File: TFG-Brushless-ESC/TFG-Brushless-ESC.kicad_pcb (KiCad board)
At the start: 4 copper layers, 110.5 x 44 mm, 147 parts, among them J1 V, J2 USB C Receptacle, J3 HALL SENSORS, J4 SWD-I2C, J5 24V IN, J6 U, J7 W, Q1 TK58E06N1, Q2 TK58E06N1, Q3 TK58E06N1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

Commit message: Added fan control and temp measurement. Not added to pcb yet
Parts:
- removed J1: V, TFG-Brushless-ESC:Screw_Terminal
- removed J7: W, TFG-Brushless-ESC:Screw_Terminal
- removed R44: 10k, Resistor_SMD:R_0603_1608Metric
- added C23: 100n, Capacitor_SMD:C_0603_1608Metric, F.Cu at (145.6, 35.2)
- added C32: 10u, Capacitor_SMD:CP_Elec_4x5.4, F.Cu at (151.5, 36.9)
- added J8: ~, TFG-Brushless-ESC:Screw_Terminal, F.Cu at (158.4, 72.9)
- added J9: ~, TFG-Brushless-ESC:Screw_Terminal, F.Cu at (188.2, 72.9)
- added L2: 30mm fan, Connector_PinHeader_1.00mm:PinHeader_1x02_P1.00mm_Vertical, F.Cu at (162.0, 36.6)
- added Q7: DMG3402L, Package_TO_SOT_SMD:SOT-23, F.Cu at (158.1, 37.4)
- added R47: 10k 1%, Resistor_SMD:R_0603_1608Metric, F.Cu at (145.6, 37.7)
- added R48: 10k, Resistor_SMD:R_0603_1608Metric, F.Cu at (145.6, 40.2)
- added R49: 22R, Resistor_SMD:R_0603_1608Metric, F.Cu at (145.6, 42.7)
- added R50: 10k, Resistor_SMD:R_0603_1608Metric, F.Cu at (160.9, 63.9)
- added R51: 10k, Resistor_SMD:R_0603_1608Metric, F.Cu at (190.6, 63.9)
- added TH1: 100k, Connector_PinHeader_1.00mm:PinHeader_1x02_P1.00mm_Vertical, F.Cu at (154.1, 41.3)
- added U11: ADC081C021, Package_TO_SOT_SMD:SOT-23-6, F.Cu at (150.0, 42.1)
- J6: value U -> ~
- R43: value 10k -> 100R; footprint Resistor_SMD:R_0603_1608Metric -> Resistor_SMD:R_0805_2012Metric
- moved R43 22.9 mm to (158.1, 41.1), turned to 0 degrees
- moved J6 0.20 mm to (128.7, 72.9), turned to 0 degrees
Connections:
- net /U renamed /Half-Bridge-U/PHASE_OUT
- net /W renamed /Half-Bridge-W/PHASE_OUT
- C30 pad 2: /V -> /Half-Bridge-V/PHASE_OUT
- C31 pad 2: /V -> /Half-Bridge-V/PHASE_OUT
- D18 pad 2: /V -> /Half-Bridge-V/PHASE_OUT
- D19 pad 2: /V -> /Half-Bridge-V/PHASE_OUT
- Q3 pad 3: /V -> /Half-Bridge-V/PHASE_OUT
- Q4 pad 2: /V -> /Half-Bridge-V/PHASE_OUT
- R28 pad 2: /V -> /Half-Bridge-V/PHASE_OUT
- R29 pad 2: /V -> /Half-Bridge-V/PHASE_OUT
- R43 pad 1: GND -> /PB7
- R43 pad 2: /V -> Net-(Q7-G)
- U6 pad 6: /V -> /Half-Bridge-V/PHASE_OUT
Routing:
- net /V: track 41.8 -> 0.00 mm, vias 5 -> 0
- net /Half-Bridge-V/PHASE_OUT: track 0.00 -> 41.8 mm, vias 0 -> 5
- net GND: track 195.6 -> 195.5 mm, vias 172 -> 186
- added copper zone on B.Cu, net /Half-Bridge-V/PHASE_OUT
- added copper zone on F.Cu, net /Half-Bridge-V/PHASE_OUT
- added copper zone on In1.Cu, net /Half-Bridge-V/PHASE_OUT
- added copper zone on In2.Cu, net /Half-Bridge-V/PHASE_OUT
- removed copper zone on B.Cu, net /V
- removed copper zone on F.Cu, net /V
- removed copper zone on In1.Cu, net /V
- removed copper zone on In2.Cu, net /V

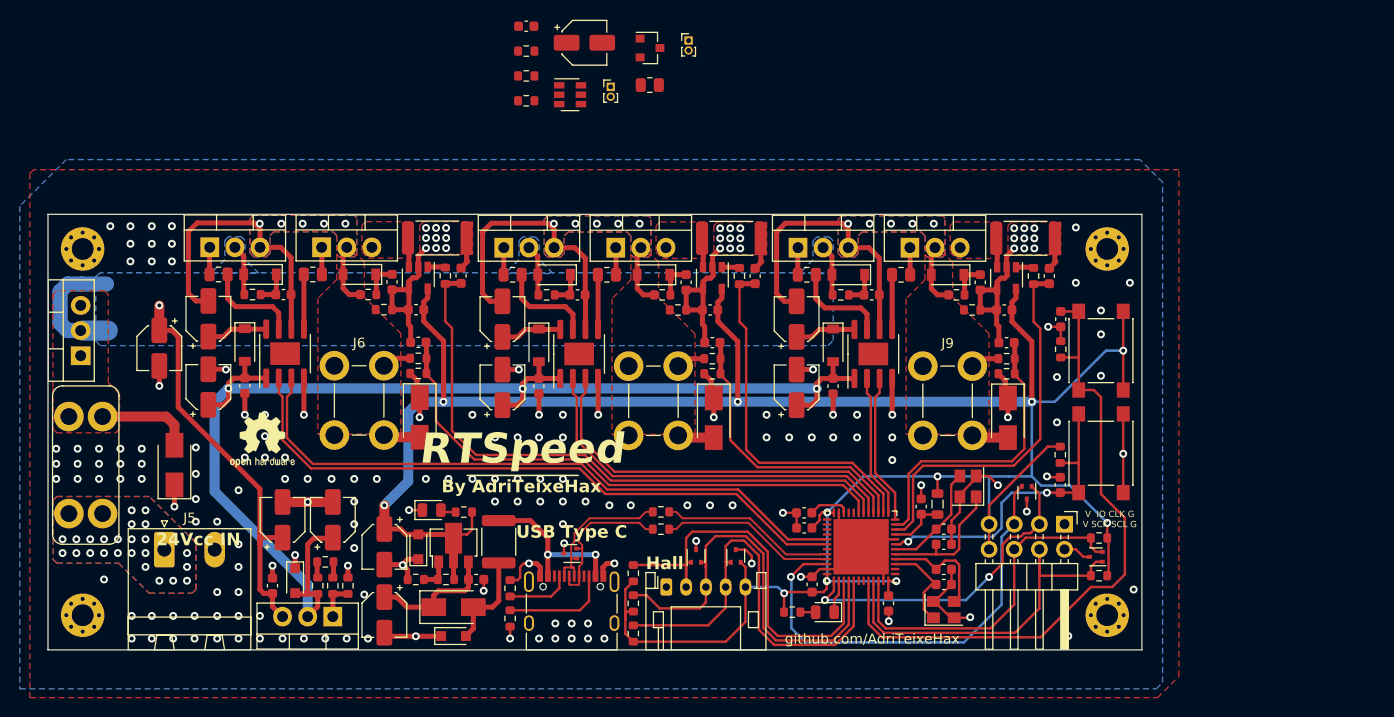
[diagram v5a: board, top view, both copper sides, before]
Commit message: Added temperature sensors per phase and adc
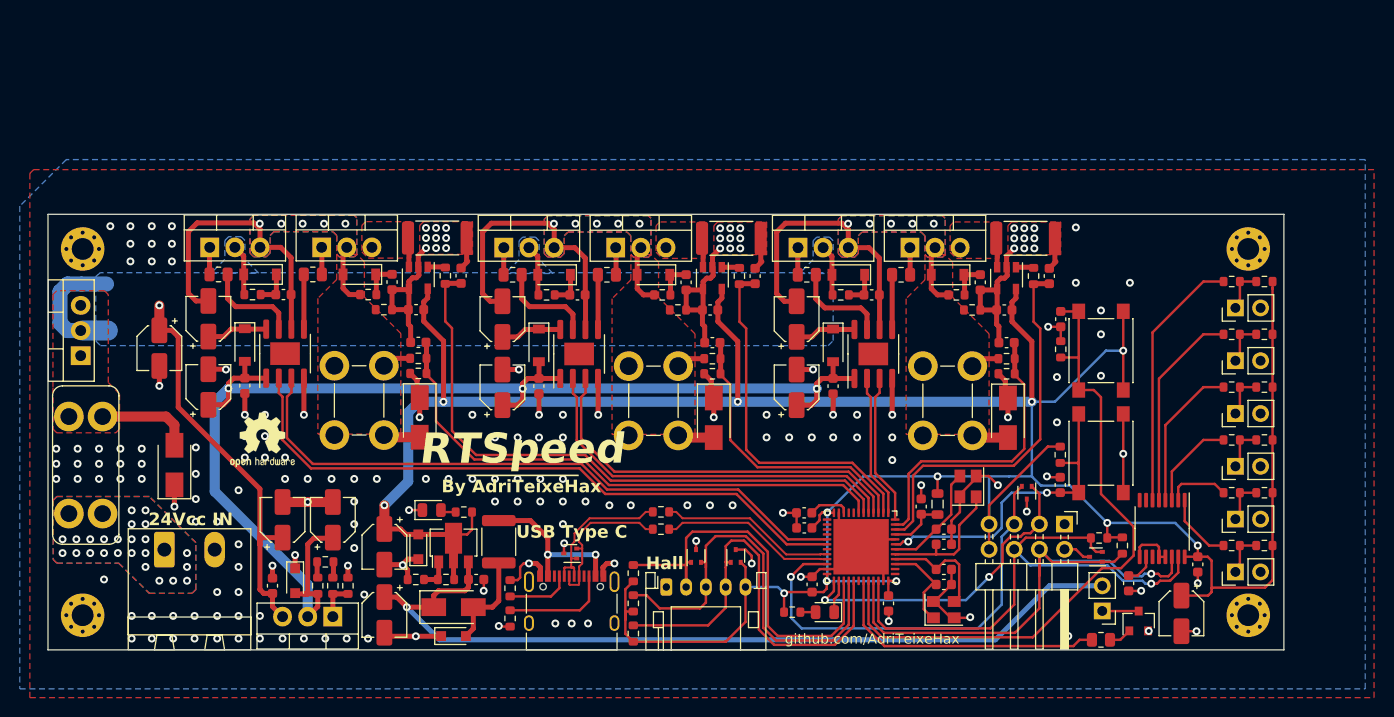
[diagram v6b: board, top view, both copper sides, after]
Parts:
- removed C23: 100n, Capacitor_SMD:C_0603_1608Metric
- removed C32: 10u, Capacitor_SMD:CP_Elec_4x5.4
- removed R47: 10k 1%, Resistor_SMD:R_0603_1608Metric
- removed R48: 10k, Resistor_SMD:R_0603_1608Metric
- removed R49: 22R, Resistor_SMD:R_0603_1608Metric
- removed TH1: 100k, Connector_PinHeader_1.00mm:PinHeader_1x02_P1.00mm_Vertical
- removed U11: ADC081C021, Package_TO_SOT_SMD:SOT-23-6
- added C46: 100n, Capacitor_SMD:C_0603_1608Metric, F.Cu at (206.5, 91.5)
- added C47: 100n, Capacitor_SMD:C_0603_1608Metric, F.Cu at (213.4, 89.6)
- added C48: 10u, Capacitor_SMD:CP_Elec_4x5.4, F.Cu at (211.8, 94.5)
- added R44: 10k 1%, Resistor_SMD:R_0603_1608Metric, F.Cu at (220.2, 87.7)
- added R52: 10k 1%, Resistor_SMD:R_0603_1608Metric, F.Cu at (220.2, 82.3)
- added R53: 22R, Resistor_SMD:R_0603_1608Metric, F.Cu at (216.9, 87.7)
- added R54: 22R, Resistor_SMD:R_0603_1608Metric, F.Cu at (216.9, 82.3)
- added R55: 10k 1%, Resistor_SMD:R_0603_1608Metric, F.Cu at (220.2, 77.0)
- added R56: 10k 1%, Resistor_SMD:R_0603_1608Metric, F.Cu at (220.2, 71.7)
- added R57: 22R, Resistor_SMD:R_0603_1608Metric, F.Cu at (216.9, 77.0)
- added R58: 22R, Resistor_SMD:R_0603_1608Metric, F.Cu at (216.9, 71.7)
- added R59: 10k 1%, Resistor_SMD:R_0603_1608Metric, F.Cu at (220.2, 66.3)
- added R60: 10k 1%, Resistor_SMD:R_0603_1608Metric, F.Cu at (220.2, 61.0)
- added R61: 22R, Resistor_SMD:R_0603_1608Metric, F.Cu at (216.9, 66.3)
- added R62: 22R, Resistor_SMD:R_0603_1608Metric, F.Cu at (216.9, 61.0)
- added TH2: 100k, Connector_PinHeader_2.54mm:PinHeader_1x02_P2.54mm_Vertical, F.Cu at (217.2, 90.3)
- added TH3: 100k, Connector_PinHeader_2.54mm:PinHeader_1x02_P2.54mm_Vertical, F.Cu at (217.2, 85.0)
- added TH4: 100k, Connector_PinHeader_2.54mm:PinHeader_1x02_P2.54mm_Vertical, F.Cu at (217.2, 79.7)
- added TH5: 100k, Connector_PinHeader_2.54mm:PinHeader_1x02_P2.54mm_Vertical, F.Cu at (217.2, 74.3)
- added TH6: 100k, Connector_PinHeader_2.54mm:PinHeader_1x02_P2.54mm_Vertical, F.Cu at (217.2, 69.0)
- added TH7: 100k, Connector_PinHeader_2.54mm:PinHeader_1x02_P2.54mm_Vertical, F.Cu at (217.2, 63.7)
- added U10: ADS7830, Package_SO:TSSOP-16_4.4x5mm_P0.65mm, F.Cu at (209.8, 85.9)
- L2: footprint Connector_PinHeader_1.00mm:PinHeader_1x02_P1.00mm_Vertical -> Connector_PinHeader_2.54mm:PinHeader_1x02_P2.54mm_Vertical
- moved Q7 76.1 mm to (207.5, 95.3), turned to 90 degrees
- moved R43 72.2 mm to (203.7, 97.2)
- moved L2 71.2 mm to (203.8, 94.3), turned to 180 degrees
- moved REF** 14.2 mm to (218.5, 57.7)
- moved REF** 14.2 mm to (218.5, 94.7)
- moved R45 3.85 mm to (205.8, 87.7), turned to 90 degrees
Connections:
- net /VDDA renamed VDDA
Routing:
- net +5V: track 13.0 -> 86.9 mm, vias 0 -> 1
- net +3V3: track 273.2 -> 328.0 mm, vias 11 -> 12
- net /PB7: track 0.00 -> 28.7 mm
- net /Temp. sensors/S6: track 0.00 -> 26.3 mm
- net /Temp. sensors/S5: track 0.00 -> 20.6 mm
- net /I2C_SDA: track 35.2 -> 55.2 mm, vias 0 -> 1
- net /I2C_SCL: track 38.5 -> 56.8 mm, vias 0 -> 1
- net /Temp. sensors/S4: track 0.00 -> 15.0 mm
- net /Temp. sensors/S3: track 0.00 -> 9.44 mm
- net GND: track 195.5 -> 204.2 mm, vias 186 -> 184
- net /Temp. sensors/S1: track 0.00 -> 7.06 mm
- net /Temp. sensors/S2: track 0.00 -> 6.40 mm
- net /Temp. sensors/T6: track 0.00 -> 4.50 mm
- net /Temp. sensors/T3: track 0.00 -> 4.50 mm
- net /Temp. sensors/T2: track 0.00 -> 4.50 mm
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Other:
- board size 110.5 x 44 mm -> 124.9 x 44 mm
- board text removed: "V IO CLK G V SCK SCL G"

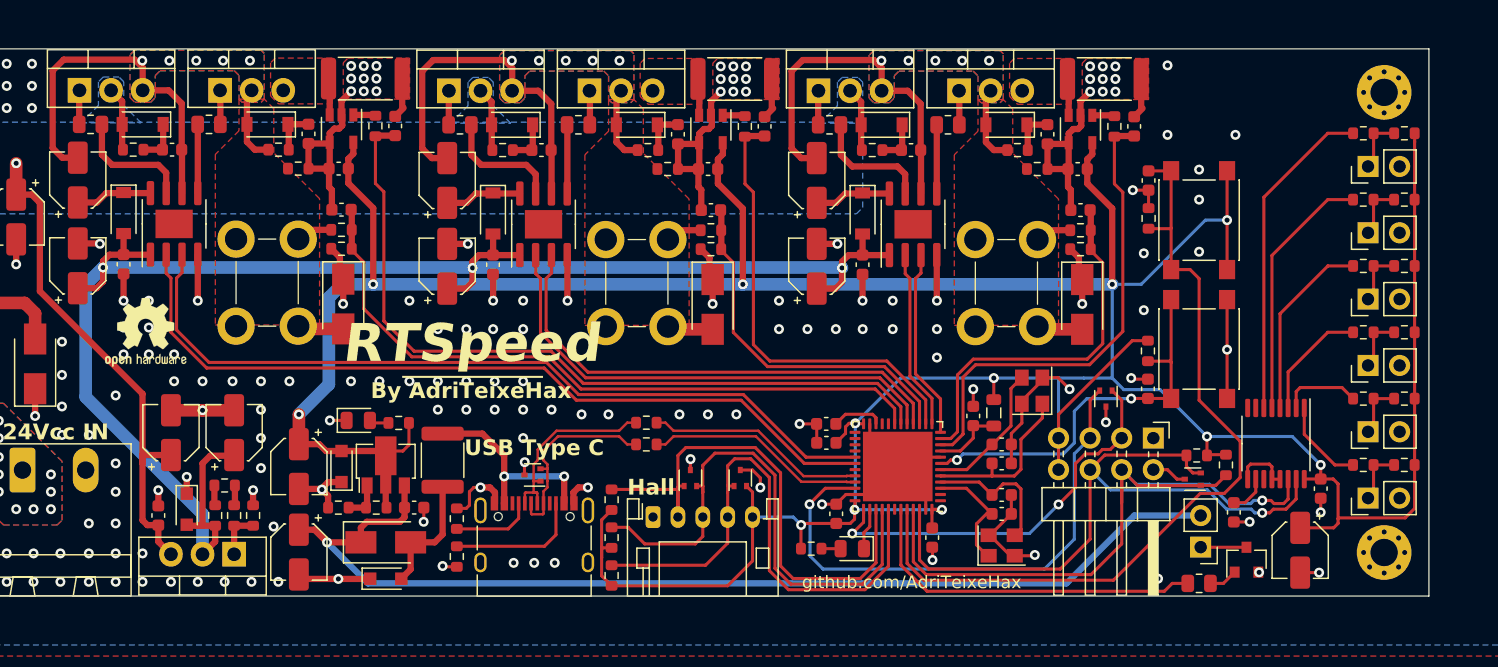
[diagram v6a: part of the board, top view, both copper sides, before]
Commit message: Added pulldown resistors for the half bridge mosfets, fan mosfet and fixed code pinout
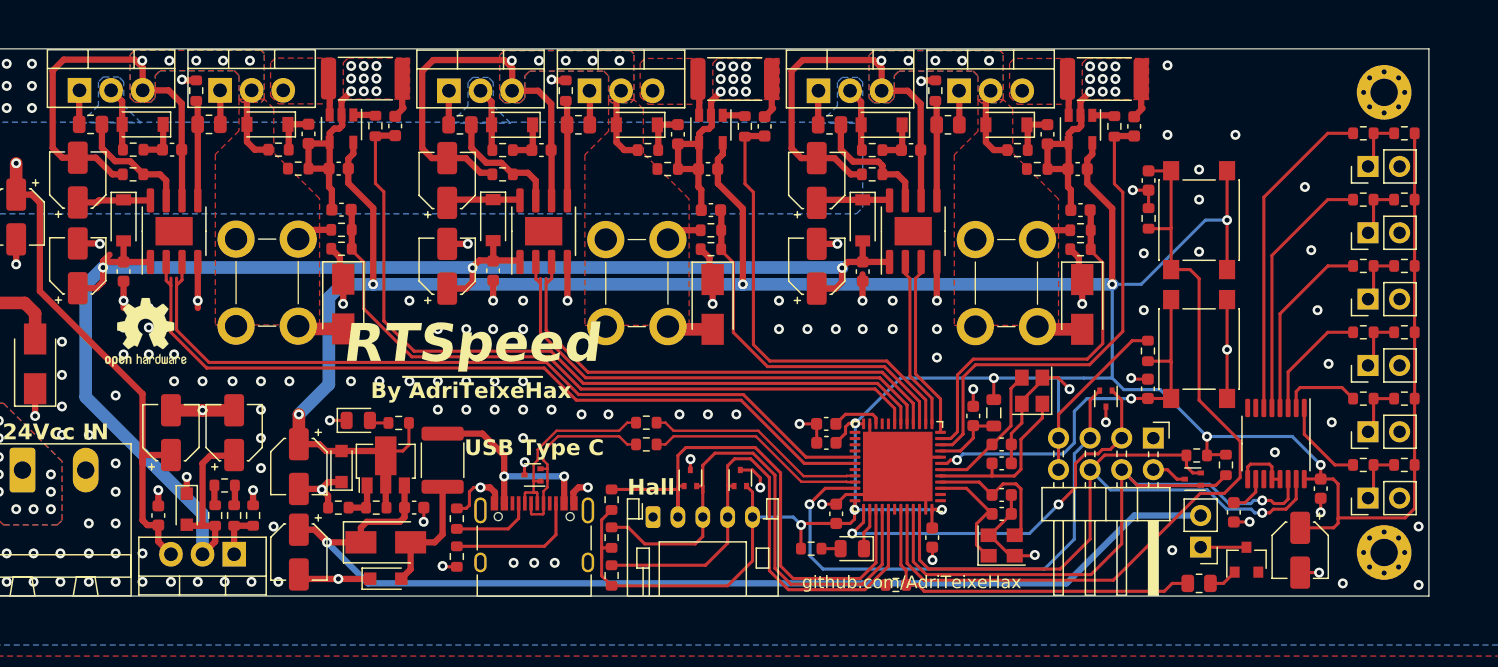
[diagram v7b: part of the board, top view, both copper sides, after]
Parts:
- added R47: 10k, Resistor_SMD:R_0603_1608Metric, F.Cu at (117.9, 64.3)
- added R48: 10k, Resistor_SMD:R_0603_1608Metric, F.Cu at (147.7, 64.3)
- added R49: 10k, Resistor_SMD:R_0603_1608Metric, F.Cu at (177.4, 64.3)
- added R63: 10k, Resistor_SMD:R_0603_1608Metric, F.Cu at (123.0, 57.6)
- added R64: 10k, Resistor_SMD:R_0603_1608Metric, F.Cu at (152.7, 57.6)
- added R65: 10k, Resistor_SMD:R_0603_1608Metric, F.Cu at (182.5, 57.6)
- added R66: 10k, Resistor_SMD:R_0603_1608Metric, F.Cu at (179.3, 97.3)
- moved C20 0.59 mm to (117.2, 72.1)
- moved D13 0.59 mm to (117.2, 68.0)
- moved U4 0.59 mm to (121.2, 68.9)
- moved C38 0.55 mm to (176.6, 72.1)
- moved D21 0.55 mm to (176.6, 68.0)
- moved U6 0.55 mm to (151.0, 68.9)
- moved U8 0.55 mm to (180.7, 68.9)
- moved D17 0.54 mm to (146.9, 68.0)
- moved C29 0.48 mm to (146.9, 72.0)
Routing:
- net /Half-Bridge-U/PHASE_OUT: track 41.8 -> 46.0 mm
- net /Half-Bridge-W/PHASE_OUT: track 41.8 -> 46.0 mm
- net /Half-Bridge-V/PHASE_OUT: track 41.8 -> 46.0 mm
- net GND: track 204.2 -> 207.2 mm, vias 184 -> 196
- net /I2C_SCL: track 56.8 -> 54.1 mm
- net Net-(U8-LO): track 5.53 -> 7.50 mm
- net Net-(U6-LO): track 5.53 -> 7.50 mm
- net Net-(U4-LO): track 5.53 -> 7.47 mm
- net +12V: track 129.1 -> 128.1 mm
- net /PB7: track 28.7 -> 29.4 mm

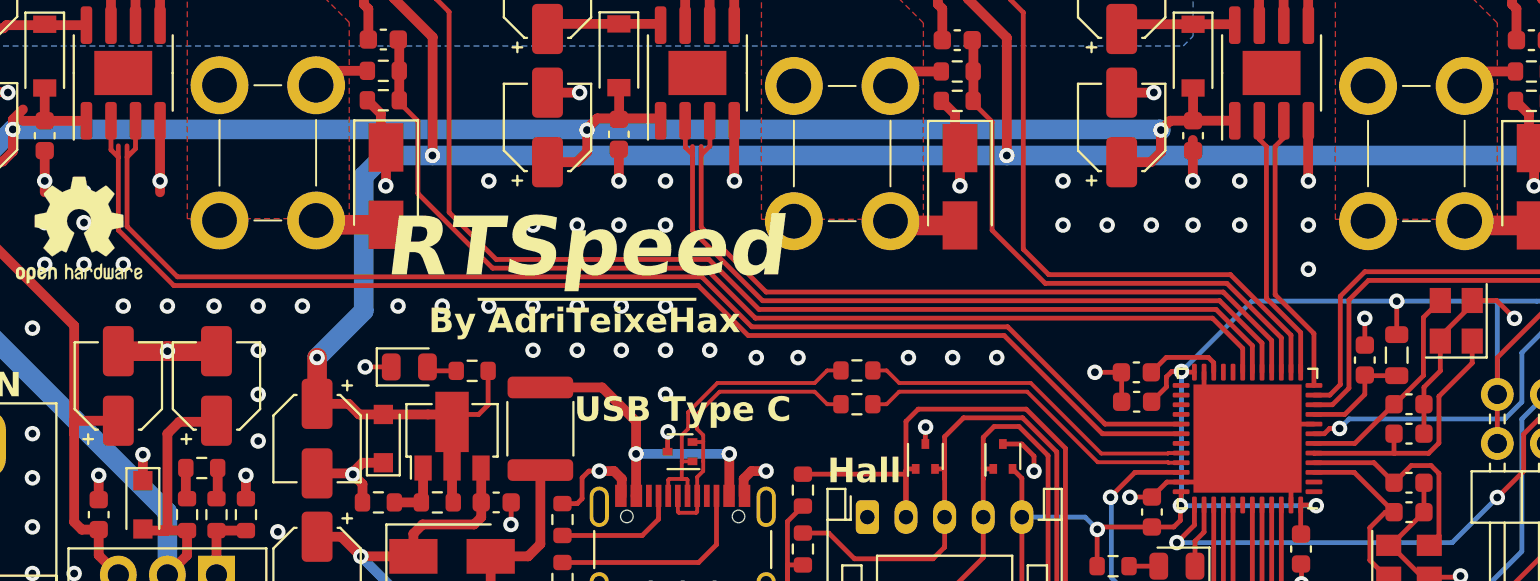
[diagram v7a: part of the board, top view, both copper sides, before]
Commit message: more separation between traces
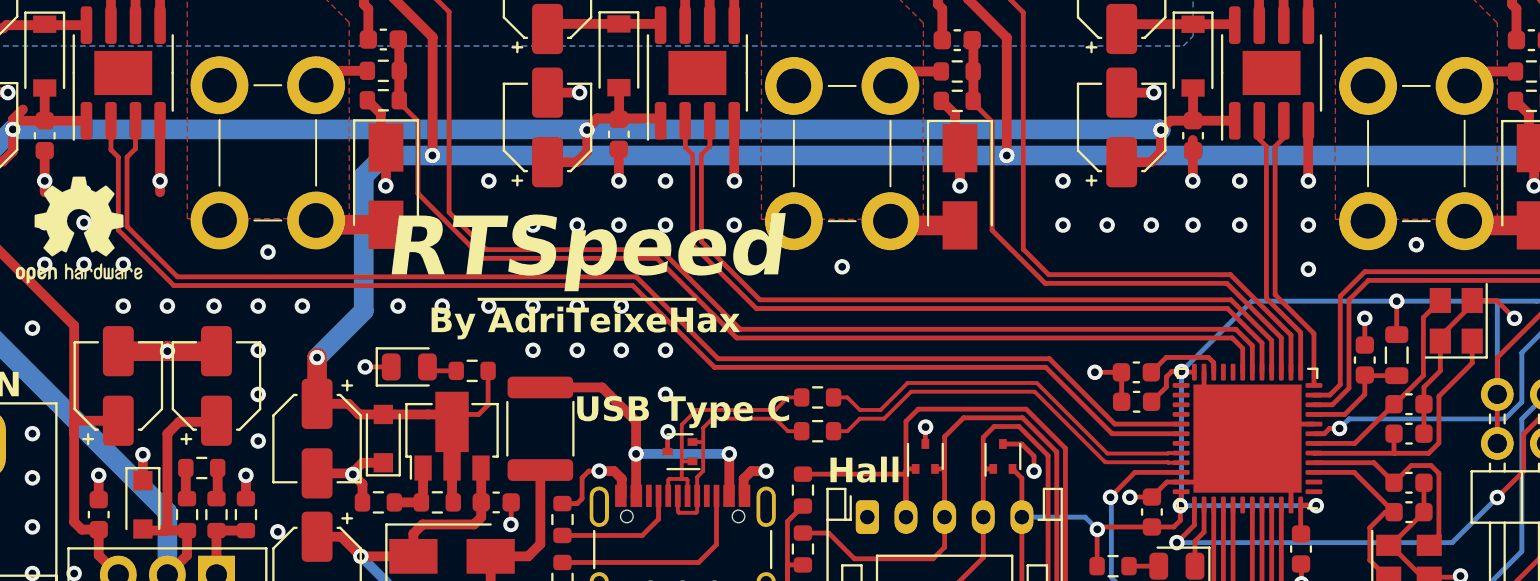
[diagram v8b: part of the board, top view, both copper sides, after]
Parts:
- moved R11 2.47 mm to (157.2, 85.7)
- moved R12 2.47 mm to (157.2, 87.4)
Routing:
- net /USB_R_P: track 16.0 -> 12.5 mm
- net /USB_R_N: track 15.9 -> 13.1 mm
- net /USB_P: track 17.7 -> 20.4 mm
- net /USB_N: track 17.7 -> 20.4 mm
- net /PA9: track 65.8 -> 65.2 mm
- net /PA8: track 65.0 -> 64.4 mm
- net GND: vias 196 -> 193
